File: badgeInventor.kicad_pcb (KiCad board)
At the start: 2 copper layers, 89.2 x 86 mm, 34 parts, among them P1 AUTO-PROGRAM JUMPER, P2 CONN_01X10, P22 CONN_01X10, P23 CONN_01X10, P3 LiPo, P5 OLED_I2C, P6 USB Serial, SW1 RESET, U1 SPX1117, U2 MCP73831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

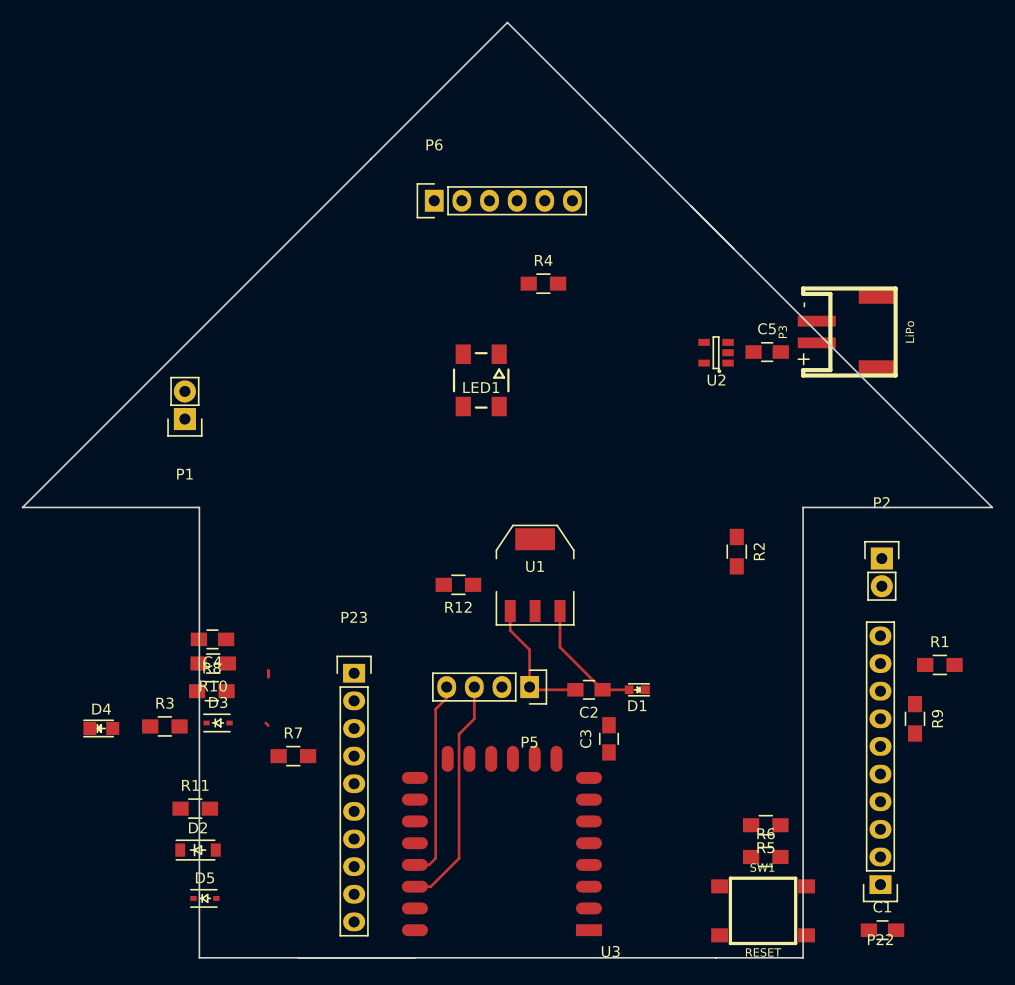
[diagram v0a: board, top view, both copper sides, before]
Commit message: Add footprint inventor
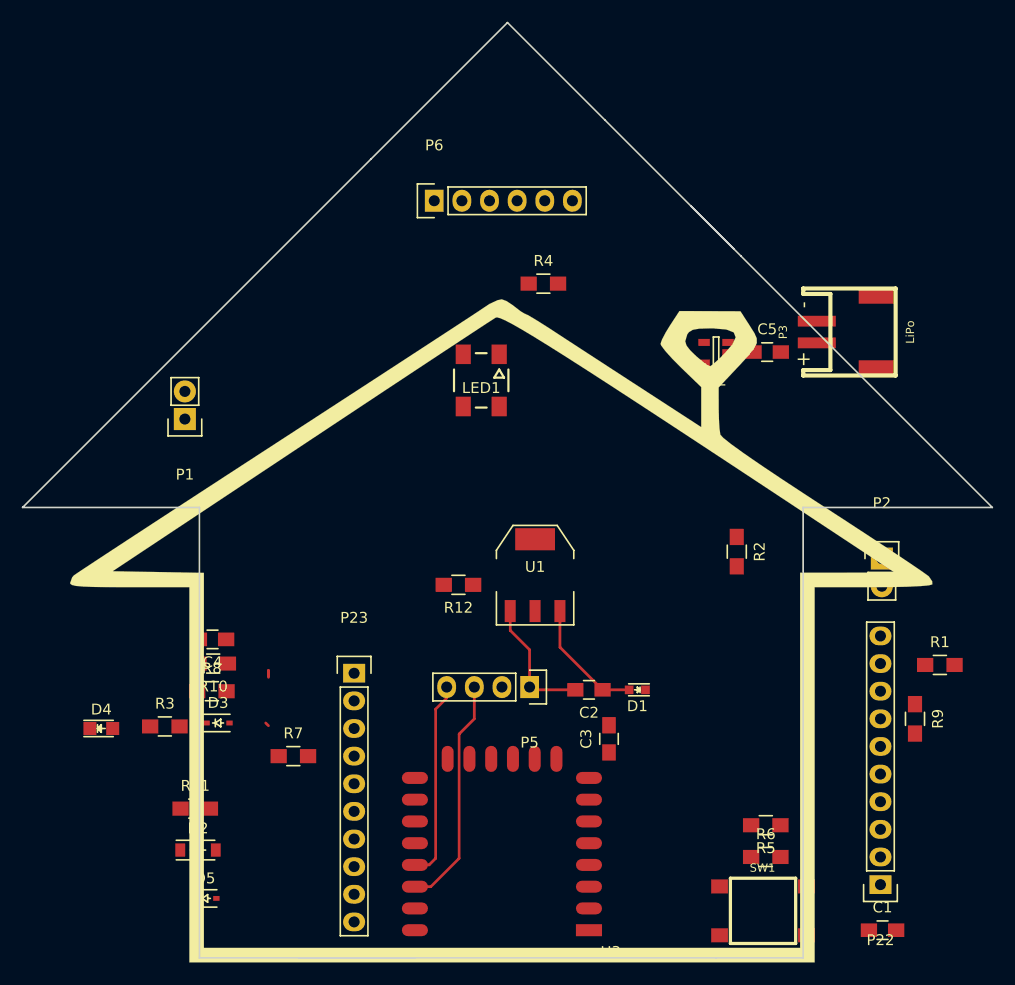
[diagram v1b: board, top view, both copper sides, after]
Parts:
- added G***: LOGO, theinventorhouse:inventor, F.Cu at (140.2, 120.0)
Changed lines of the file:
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@@
-(kicad_pcb (version 4) (host pcbnew 4.0.0-rc1-stable)
+(kicad_pcb (version 4) (host pcbnew 4.0.0~rc1a-stable)
   (general
-    (links 84)
+    (links 0)
     (no_connects 78)
-    (area 96.190999 64.821999 202.500572 178.278244)
+    (area 96.190999 64.821999 214.517375 161.450001)
     (thickness 1.6)
     (drawings 15)
     (tracks 31)
     (zones 0)
-    (modules 34)
+    (modules 35)
     (nets 35)
   )
@@
     )
   )
+  (module theinventorhouse:inventor (layer F.Cu)
+    (at 140.208 120.015)
+    (fp_text reference G*** (at 0 0) (layer F.SilkS) hide
+      (effects (font (thickness 0.3)))
+    )
+    (fp_text value LOGO (at 0.75 0) (layer F.SilkS) hide
+      (effects (font (thickness 0.3)))
+    )
+    (fp_poly (pts (xy 0.552061 -29.515924) (xy 1.156882 -29.11576) (xy 1.288082 -29.009474) (xy 1.842459 -28.580138)
+      (xy 2.222811 -28.352212) (xy 2.270231 -28.341053) (xy 2.559007 -28.203061) (xy 3.190062 -27.830516)
+      (xy 4.0608 -27.285565) (xy 4.771635 -26.825861) (xy 5.664279 -26.242543) (xy 6.908697 -25.431148)
+      (xy 8.408101 -24.454688) (xy 10.065701 -23.37618) (xy 11.784708 -22.258637) (xy 12.766842 -21.620582)
+      (xy 18.448421 -17.930494) (xy 18.448421 -21.606647) (xy 16.576842 -23.413504) (xy 15.773508 -24.224152)
+      (xy 15.142756 -24.927432) (xy 14.769835 -25.424635) (xy 14.705263 -25.580655) (xy 14.784106 -25.812019)
+      (xy 16.975934 -25.812019) (xy 17.103809 -25.414518) (xy 17.439717 -24.987021) (xy 17.991726 -24.448093)
+      (xy 18.598151 -23.937921) (xy 19.097308 -23.596694) (xy 19.275712 -23.531386) (xy 19.534026 -23.704897)
+      (xy 20.041062 -24.157701) (xy 20.545712 -24.650659) (xy 21.312014 -25.533163) (xy 21.61305 -26.186518)
+      (xy 21.436323 -26.633629) (xy 20.769332 -26.897398) (xy 19.59958 -27.00073) (xy 19.261367 -27.00421)
+      (xy 18.26875 -26.977563) (xy 17.667136 -26.873112) (xy 17.31437 -26.654096) (xy 17.169782 -26.463316)
+      (xy 16.975934 -25.812019) (xy 14.784106 -25.812019) (xy 14.843684 -25.986845) (xy 15.20181 -26.665367)
+      (xy 15.574211 -27.26988) (xy 16.443158 -28.598813) (xy 19.250526 -28.588038) (xy 22.057895 -28.577262)
+      (xy 22.93237 -27.217506) (xy 23.329555 -26.586692) (xy 23.550438 -26.101773) (xy 23.560887 -25.663112)
+      (xy 23.326768 -25.17107) (xy 22.813949 -24.52601) (xy 21.988297 -23.628292) (xy 21.539414 -23.15129)
+      (xy 20.052632 -21.571001) (xy 20.056282 -19.6755) (xy 20.078169 -18.644419) (xy 20.132014 -17.767639)
+      (xy 20.20564 -17.237734) (xy 20.475818 -16.93828) (xy 21.191523 -16.36944) (xy 22.341159 -15.539282)
+      (xy 23.913128 -14.455871) (xy 25.895833 -13.127277) (xy 28.277677 -11.561565) (xy 29.622527 -10.687207)
+      (xy 31.63745 -9.377506) (xy 33.52478 -8.14323) (xy 35.234354 -7.017738) (xy 36.716012 -6.034387)
+      (xy 37.919593 -5.226535) (xy 38.794935 -4.627541) (xy 39.291877 -4.270762) (xy 39.375553 -4.2013)
+      (xy 39.683826 -3.752616) (xy 39.698183 -3.466037) (xy 39.384911 -3.380152) (xy 38.60215 -3.308397)
+      (xy 37.415032 -3.253828) (xy 35.888691 -3.219501) (xy 34.207379 -3.208421) (xy 28.87579 -3.208421)
+      (xy 28.87579 31.282105) (xy -28.608421 31.282105) (xy -28.608421 -3.208421) (xy -34.089474 -3.208421)
+      (xy -35.965903 -3.21348) (xy -37.371249 -3.231677) (xy -38.369097 -3.267542) (xy -39.023032 -3.325605)
+      (xy -39.396638 -3.410397) (xy -39.553499 -3.526448) (xy -39.570526 -3.598932) (xy -39.38599 -4.112385)
+      (xy -39.236316 -4.287467) (xy -38.965225 -4.476041) (xy -38.661016 -4.678947) (xy -35.661298 -4.678947)
+      (xy -31.466438 -4.605316) (xy -27.271579 -4.531685) (xy -27.271579 29.945263) (xy 27.538947 29.945263)
+      (xy 27.538947 -4.545263) (xy 31.883684 -4.550467) (xy 36.228421 -4.55567) (xy 26.870526 -10.743055)
+      (xy 22.728514 -13.479473) (xy 19.009448 -15.931318) (xy 15.692214 -18.111935) (xy 12.7557 -20.034668)
+      (xy 10.178792 -21.712861) (xy 7.940376 -23.15986) (xy 6.01934 -24.389007) (xy 4.394569 -25.413649)
+      (xy 3.044951 -26.247128) (xy 1.949372 -26.90279) (xy 1.086718 -27.393978) (xy 0.435876 -27.734038)
+      (xy -0.024267 -27.936314) (xy -0.314824 -28.014149) (xy -0.432751 -27.999651) (xy -0.730732 -27.812218)
+      (xy -1.43897 -27.35193) (xy -2.52239 -26.641945) (xy -3.945918 -25.705418) (xy -5.674477 -24.565505)
+      (xy -7.672993 -23.245363) (xy -9.906389 -21.768146) (xy -12.339589 -20.15701) (xy -14.93752 -18.435113)
+      (xy -17.665104 -16.625608) (xy -18.298544 -16.205145) (xy -35.661298 -4.678947) (xy -38.661016 -4.678947)
+      (xy -38.279442 -4.933454) (xy -37.212885 -5.637524) (xy -35.799469 -6.566068) (xy -34.073114 -7.696905)
+      (xy -32.067736 -9.007852) (xy -29.817253 -10.476728) (xy -27.355581 -12.08135) (xy -24.716639 -13.799537)
+      (xy -21.934343 -15.609107) (xy -20.453684 -16.571343) (xy -17.612499 -18.417767) (xy -14.898246 -20.182707)
+      (xy -12.344704 -21.844141) (xy -9.985651 -23.380043) (xy -7.854865 -24.76839) (xy -5.986124 -25.987158)
+      (xy -4.413206 -27.014322) (xy -3.16989 -27.827859) (xy -2.289954 -28.405744) (xy -1.807176 -28.725953)
+      (xy -1.72428 -28.783335) (xy -1.013553 -29.256226) (xy -0.292764 -29.589689) (xy 0.109542 -29.677895)
+      (xy 0.552061 -29.515924)) (layer F.SilkS) (width 0.01))
+  )
   (dimension 85.853503 (width 0.3) (layer Margin)

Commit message: Edge Cut
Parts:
- P3: moved to B.Cu
- moved C1 41.6 mm to (151.5, 114.2)
- moved P6 41.0 mm to (136.8, 122.2)
- moved P3 40.9 mm to (138.5, 108.2), turned to 270 degrees
- moved R4 36.0 mm to (116.4, 111.8)
- moved D4 22.6 mm to (120.4, 114.8)
- moved C5 19.6 mm to (146.7, 102.9)
- moved P2 18.9 mm to (156.5, 112.4)
- moved P22 18.8 mm to (156.3, 145.0)
- moved P1 17.7 mm to (127.8, 107.7)
- moved R1 17.4 mm to (163.4, 126.4)
- moved R9 17.1 mm to (165.5, 117.6)
- moved R3 15.8 mm to (121.1, 119.0)
- moved U2 11.7 mm to (152.6, 104.3)
- moved D2 7.73 mm to (120.1, 141.0)
- moved R11 7.24 mm to (119.4, 137.3)
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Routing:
- net +3V3: track 1.24 -> 0.12 mm
- net (no net): track 1.50 -> 2.40 mm
- net /ESP8266/RST: track 0.66 -> 0.00 mm
- net /ESP8266/ADC_IN: track 0.54 -> 0.00 mm
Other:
- board size 89.2 x 86 mm -> 40.6 x 26.6 mm
